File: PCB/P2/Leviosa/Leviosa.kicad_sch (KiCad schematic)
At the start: 50 parts, among them J1 Barrel_Jack, J2 2.54mm 1x03 Spare, U5 LM393

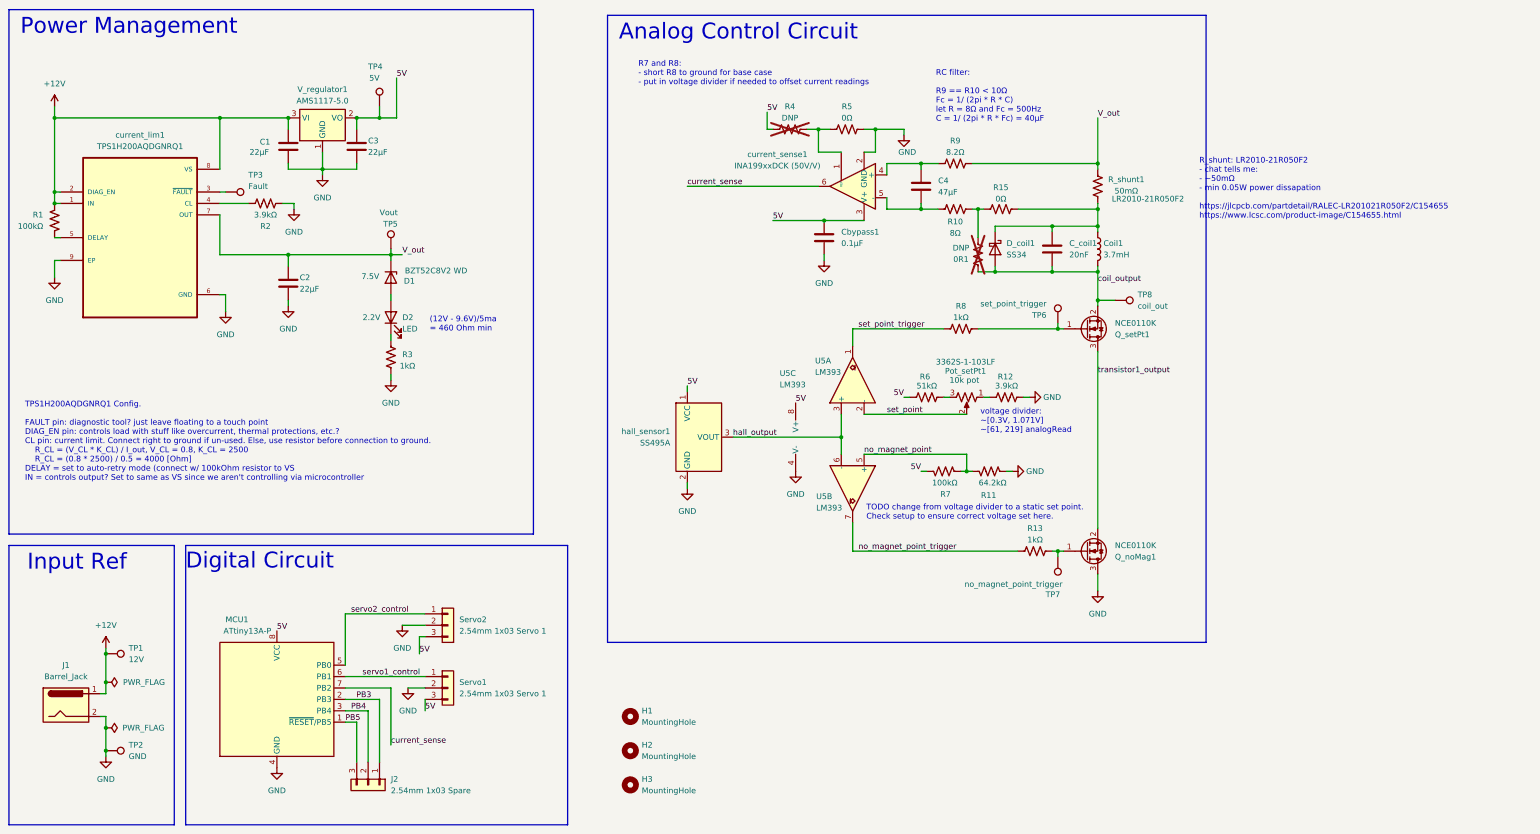
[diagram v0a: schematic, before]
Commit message: update a resistor and PCB
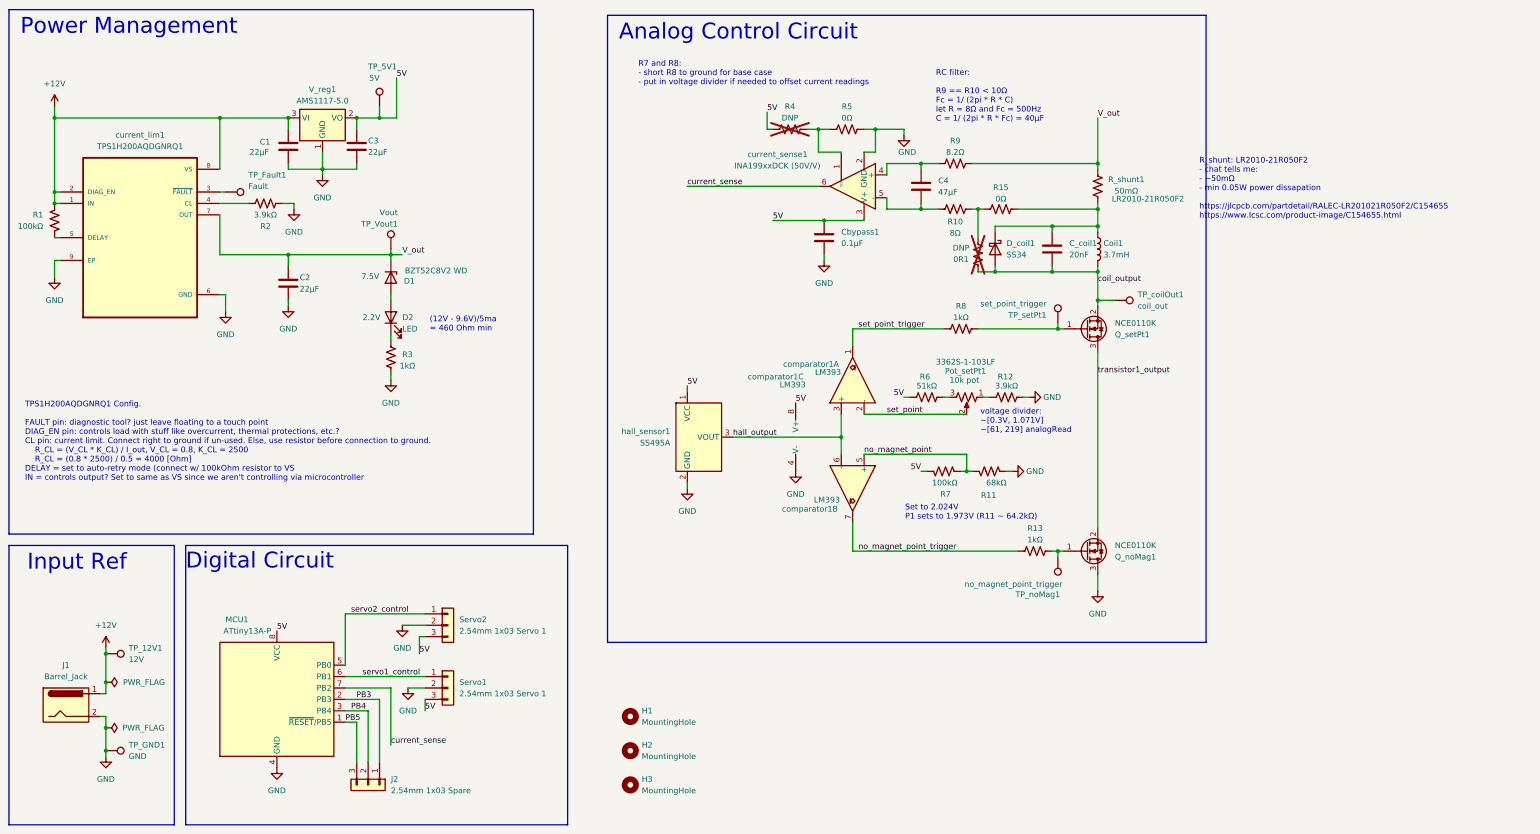
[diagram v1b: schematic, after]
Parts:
- R11: value 64.2kΩ -> 68kΩ; footprint Resistor_SMD:R_0805_2012Metric_Pad1.20x1.40mm_HandSolder -> Resistor_SMD:R_0603_1608Metric; Link (none) -> https://jlcpcb.com/partdetail/23958-0603WAF6802T5E/C23231
- renumbered TP1 to TP_12V1, TP4 to TP_5V1, TP3 to TP_Fault1, TP2 to TP_GND1, TP5 to TP_Vout1, TP8 to TP_coilOut1, TP7 to TP_noMag1, TP6 to TP_setPt1, V_regulator1 to V_reg1, U5 to comparator1
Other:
- note added: "Set to 2.024V P1 sets to 1.973V (R11 ~ 64.2kΩ)"
- note removed: "TODO change from voltage divider to a static set point. Check setup to ensure correct voltage set here."
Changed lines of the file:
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@@
 		)
 	)
-	(text "TODO change from voltage divider to a static set point.\nCheck setup to ensure correct voltage set here."
+	(text "Set to 2.024V\nP1 sets to 1.973V (R11 ~ 64.2kΩ)"
 		(exclude_from_sim no)
-		(at 204.978 127.762 0)
+		(at 213.614 127.762 0)
 		(effects
 			(font
@@
 		(on_board yes)
 		(dnp no)
-		(property "Reference" "TP4"
+		(property "Reference" "TP_5V1"
 			(at 93.98 26.67 0)
 			(effects
@@
 			(project "Leviosa"
 				(path "/fe766911-203b-467c-b704-d4bd488f6c98"
-					(reference "TP4")
+					(reference "TP_5V1")
 					(unit 1)
 				)
@@
 			)
 		)
-		(property "Value" "64.2kΩ"
+		(property "Value" "68kΩ"
 			(at 236.22 119.38 90)
 			(effects
@@
 			)
 		)
-		(property "Footprint" "Resistor_SMD:R_0805_2012Metric_Pad1.20x1.40mm_HandSolder"
+		(property "Footprint" "Resistor_SMD:R_0603_1608Metric"
 			(at 232.156 115.824 90)
 			(effects
@@
 			)
 		)
-		(property "Link" ""
+		(property "Link" "https://jlcpcb.com/partdetail/23958-0603WAF6802T5E/C23231"
 			(at 232.41 116.84 0)
 			(effects
@@
 		(dnp no)
 		(fields_autoplaced yes)
-		(property "Reference" "TP2"
+		(property "Reference" "TP_GND1"
 			(at 40.64 177.7999 90)
 			(effects
@@
 			(project "Leviosa"
 				(path "/fe766911-203b-467c-b704-d4bd488f6c98"
-					(reference "TP2")
+					(reference "TP_GND1")
 					(unit 1)
 				)
@@
 		(on_board yes)
 		(dnp no)
-		(property "Reference" "TP7"
+		(property "Reference" "TP_noMag1"
 			(at 248.158 144.272 0)
 			(effects
@@
 			(project "Leviosa"
 				(path "/fe766911-203b-467c-b704-d4bd488f6c98"
-					(reference "TP7")
+					(reference "TP_noMag1")
 					(unit 1)
 				)
@@
 		(dnp no)
 		(fields_autoplaced yes)
-		(property "Reference" "V_regulator1"
+		(property "Reference" "V_reg1"
 			(at 83.82 31.75 0)
 			(effects
@@
 			(project ""
 				(path "/fe766911-203b-467c-b704-d4bd488f6c98"
-					(reference "V_regulator1")
+					(reference "V_reg1")
 					(unit 1)
 				)
@@
 		(on_board yes)
 		(dnp no)
-		(property "Reference" "TP6"
+		(property "Reference" "TP_setPt1"
 			(at 245.11 82.042 0)
 			(effects
@@
 			(project "Leviosa"
 				(path "/fe766911-203b-467c-b704-d4bd488f6c98"
-					(reference "TP6")
+					(reference "TP_setPt1")
 					(unit 1)
 				)
@@
 		(on_board yes)
 		(dnp no)
-		(property "Reference" "TP3"
+		(property "Reference" "TP_Fault1"
 			(at 67.31 50.8 90)
 			(effects
@@
 			(project "Leviosa"
 				(path "/fe766911-203b-467c-b704-d4bd488f6c98"
-					(reference "TP3")
+					(reference "TP_Fault1")
 					(unit 1)
 				)
@@
 		(on_board yes)
 		(dnp no)
-		(property "Reference" "TP5"
+		(property "Reference" "TP_Vout1"
 			(at 100.584 61.722 0)
 			(effects
@@
 			(project "Leviosa"
 				(path "/fe766911-203b-467c-b704-d4bd488f6c98"
-					(reference "TP5")
+					(reference "TP_Vout1")
 					(unit 1)
 				)
@@
 		(on_board yes)
 		(dnp no)
-		(property "Reference" "U5"
-			(at 193.802 122.428 90)
+		(property "Reference" "comparator1"
+			(at 186.182 125.222 90)
 			(effects
 				(font
@@
 		)
 		(property "Value" "LM393"
-			(at 193.802 124.968 90)
+			(at 193.294 123.19 90)
 			(effects
 				(font
@@
 			(project ""
 				(path "/fe766911-203b-467c-b704-d4bd488f6c98"
-					(reference "U5")
+					(reference "comparator1")
 					(unit 2)
 				)
@@
 		(on_board yes)
 		(dnp no)
-		(property "Reference" "TP8"
+		(property "Reference" "TP_coilOut1"
 			(at 265.43 77.47 90)
 			(effects
@@
 			(project "Leviosa"
 				(path "/fe766911-203b-467c-b704-d4bd488f6c98"
-					(reference "TP8")
+					(reference "TP_coilOut1")
 					(unit 1)
 				)
@@
 		(dnp no)
 		(fields_autoplaced yes)
-		(property "Reference" "TP1"
+		(property "Reference" "TP_12V1"
 			(at 40.64 156.2099 90)
 			(effects
@@
 			(project "Leviosa"
 				(path "/fe766911-203b-467c-b704-d4bd488f6c98"
-					(reference "TP1")
+					(reference "TP_12V1")
 					(unit 1)
 				)
@@
 		(on_board yes)
 		(dnp no)
-		(property "Reference" "U5"
-			(at 185.674 94.996 0)
+		(property "Reference" "comparator1"
+			(at 178.562 95.758 0)
 			(effects
 				(font
@@
 			(project ""
 				(path "/fe766911-203b-467c-b704-d4bd488f6c98"
-					(reference "U5")
+					(reference "comparator1")
 					(unit 3)
 				)
@@
 		(on_board yes)
 		(dnp no)
-		(property "Reference" "U5"
-			(at 193.548 92.202 90)
+		(property "Reference" "comparator1"
+			(at 186.436 92.964 90)
 			(effects
 				(font
@@
 			(project ""
 				(path "/fe766911-203b-467c-b704-d4bd488f6c98"
-					(reference "U5")
+					(reference "comparator1")
 					(unit 1)
 				)

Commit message: Update schematic layout for clarity
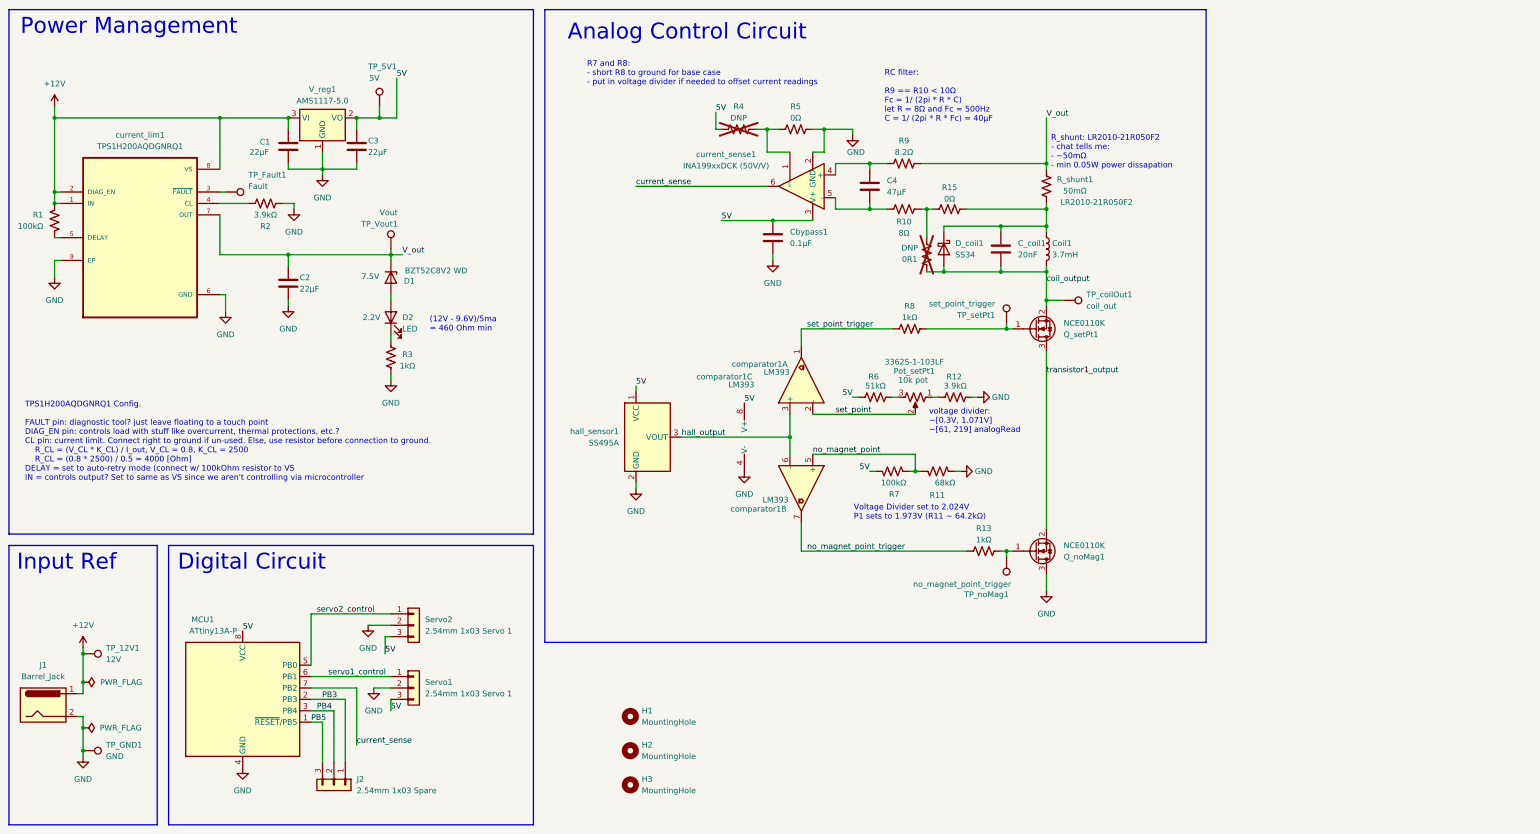
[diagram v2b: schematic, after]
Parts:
- R_shunt1: Link (none) -> https://jlcpcb.com/partdetail/RALEC-LR201021R050F2/C154655; Link2 (none) -> https://www.lcsc.com/product-image/C154655.html
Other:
- note added: "R_shunt: LR2010-21R050F2 - chat tells me: - ~50mΩ - min 0.05W power dissapation"
- note added: "Voltage Divider set to 2.024V P1 sets to 1.973V (R11 ~ 64.2kΩ)"
- note removed: "R_shunt: LR2010-21R050F2 - chat tells me: - ~50mΩ - min 0.05W power dissapation https://jlcpcb.com/partdetail/RALEC-LR201021R050F2/C154655 https://www.lcsc.com/product-image/C154655.html"
- note removed: "Set to 2.024V P1 sets to 1.973V (R11 ~ 64.2kΩ)"
- moved on the sheet: 0R1, C4, C_coil1, Cbypass1, Coil1, D_coil1, J1, J2, MCU1, Pot_setPt1, Q_noMag1, Q_setPt1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

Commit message: added cap to attiny and fixed resistors to 8.2R
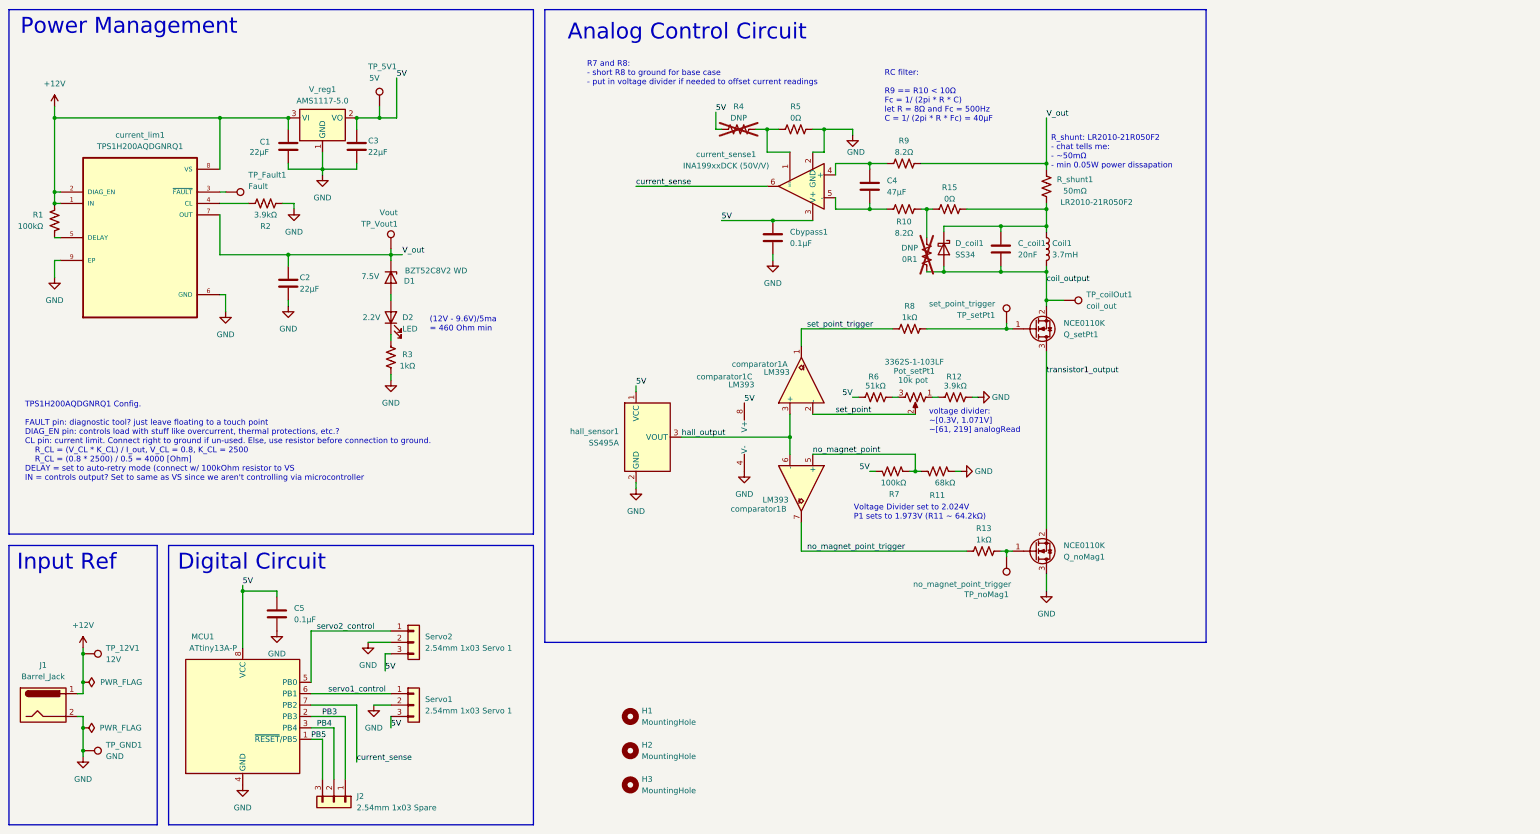
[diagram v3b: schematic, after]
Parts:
- added C5: 0.1µF, Capacitor_SMD:C_0402_1005Metric, symbol Device:C
- R10: value 8Ω -> 8.2Ω
- R_shunt1: Link https://jlcpcb.com/partdetail/RALEC-LR201021R050F2/C154655 -> https://www.lcsc.com/product-detail/C7467249.html?s_z=n_LR2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; Link2 https://www.lcsc.com/product-image/C154655.html -> https://www.lcsc.com/product-detail/C7467249.html?s_z=n_LR2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
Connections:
- net 5V: now also C5.1
- net GND: now also C5.2
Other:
- moved on the sheet: J2, MCU1, Servo1, Servo2

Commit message: update schematic and pcb per Jack's feedback
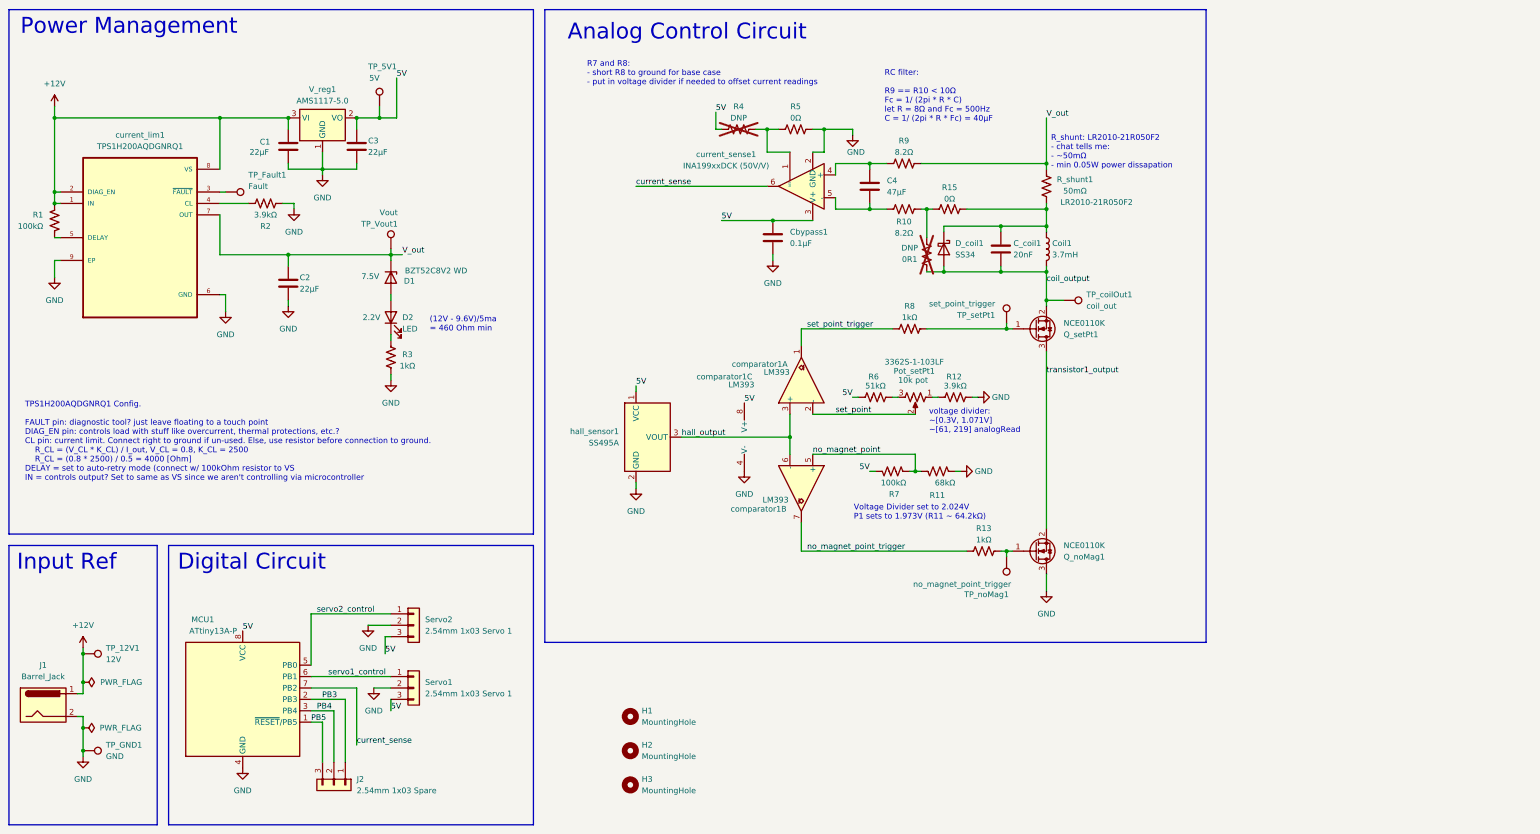
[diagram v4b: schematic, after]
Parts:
- removed C5: 0.1µF, Capacitor_SMD:C_0402_1005Metric, symbol Device:C
- R_shunt1: Link https://www.lcsc.com/product-detail/C7467249.html?s_z=n_LR2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 -> https://jlcpcb.com/partdetail/RALEC-LR201021R050F2/C154655; Link2 https://www.lcsc.com/product-detail/C7467249.html?s_z=n_LR2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 -> https://www.lcsc.com/product-image/C154655.html
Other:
- moved on the sheet: J2, MCU1, Servo1, Servo2

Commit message: add fiducials and add thickness to 5V
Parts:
- added Cbypass2: 0.1µF, Capacitor_SMD:C_0402_1005Metric, symbol Device:C
- added FID1, FID2, FID3: Fiducial, Fiducial:Fiducial_0.5mm_Mask1mm, symbol Mechanical:Fiducial
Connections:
- net 5V: now also Cbypass2.1
- net GND: now also Cbypass2.2
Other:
- moved on the sheet: J2, MCU1, Servo1, Servo2
